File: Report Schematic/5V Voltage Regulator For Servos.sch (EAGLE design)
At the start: 3 parts, among them IC2 7805T

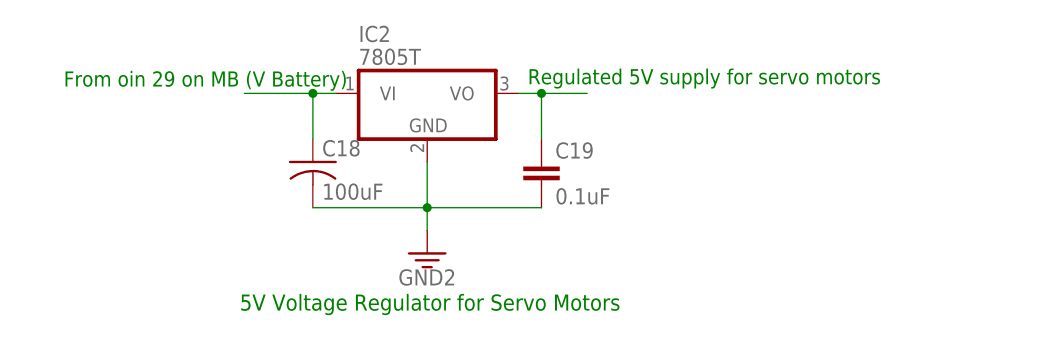
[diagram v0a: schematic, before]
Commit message: Powering and reset switch circuit added to manual
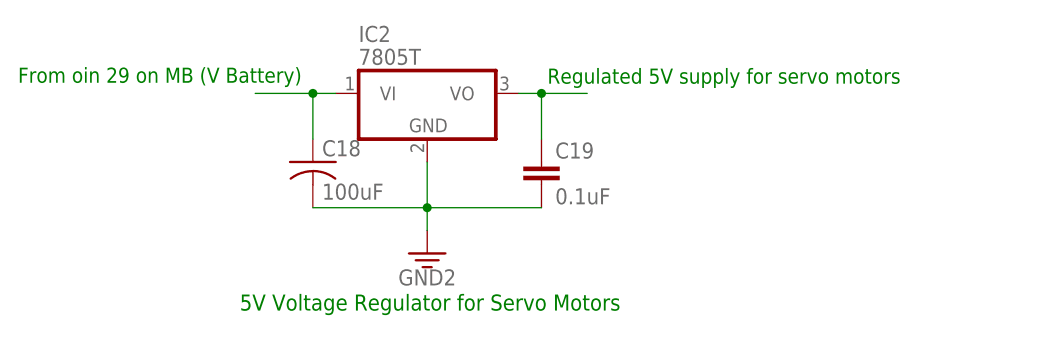
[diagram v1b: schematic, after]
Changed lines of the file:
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@@
 <setting verticaltext="up"/>
 </settings>
-<grid distance="0.01" unitdist="inch" unit="inch" style="lines" multiple="1" display="no" altdistance="0.01" altunitdist="inch" altunit="inch"/>
+<grid distance="0.0001" unitdist="inch" unit="inch" style="lines" multiple="1" display="no" altdistance="0.01" altunitdist="inch" altunit="inch"/>
 <layers>
 <layer number="1" name="Top" color="4" fill="1" visible="no" active="no"/>
@@
 <plain>
 <text x="32.512" y="39.37" size="1.778" layer="91">5V Voltage Regulator for Servo Motors</text>
-<text x="12.954" y="64.262" size="1.6764" layer="91">From oin 29 on MB (V Battery)</text>
-<text x="64.516" y="64.516" size="1.6764" layer="91">Regulated 5V supply for servo motors</text>
+<text x="7.874" y="64.6811" size="1.6764" layer="91">From oin 29 on MB (V Battery)</text>
+<text x="66.69531875" y="64.5795" size="1.6764" layer="91">Regulated 5V supply for servo motors</text>
 </plain>
 <instances>
@@
 <pinref part="C18" gate="G$1" pin="1"/>
 <wire x1="40.64" y1="63.5" x2="40.64" y2="58.42" width="0.1524" layer="91"/>
-<wire x1="40.64" y1="63.5" x2="33.02" y2="63.5" width="0.1524" layer="91"/>
+<wire x1="40.64" y1="63.5" x2="34.229040625" y2="63.5" width="0.1524" layer="91"/>
 <junction x="40.64" y="63.5"/>
 </segment>
